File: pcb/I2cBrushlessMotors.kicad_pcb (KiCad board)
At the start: 2 copper layers, 50 x 50 mm, 65 parts, among them J1 Conn_01x03, J2 Conn_01x06, J3 Header, J4 Socket, J5 Conn_01x03, Q1 Q_PMOS_GSD, Q10 Q_PMOS_GSD, Q11 Q_NMOS_GSD, Q12 Q_NMOS_GSD, Q13 Q_PMOS_GSD, Q14 Q_NMOS_GSD, Q15 Q_NMOS_GSD, Q16 Q_PMOS_GSD, Q17 Q_NMOS_GSD, Q18 Q_NMOS_GSD, Q2 Q_NMOS_GSD, Q3 Q_NMOS_GSD, Q4 Q_PMOS_GSD, Q5 Q_NMOS_GSD, Q6 Q_NMOS_GSD, Q7 Q_PMOS_GSD, Q8 Q_NMOS_GSD, Q9 Q_NMOS_GSD, U1 ATmega328PB-MU

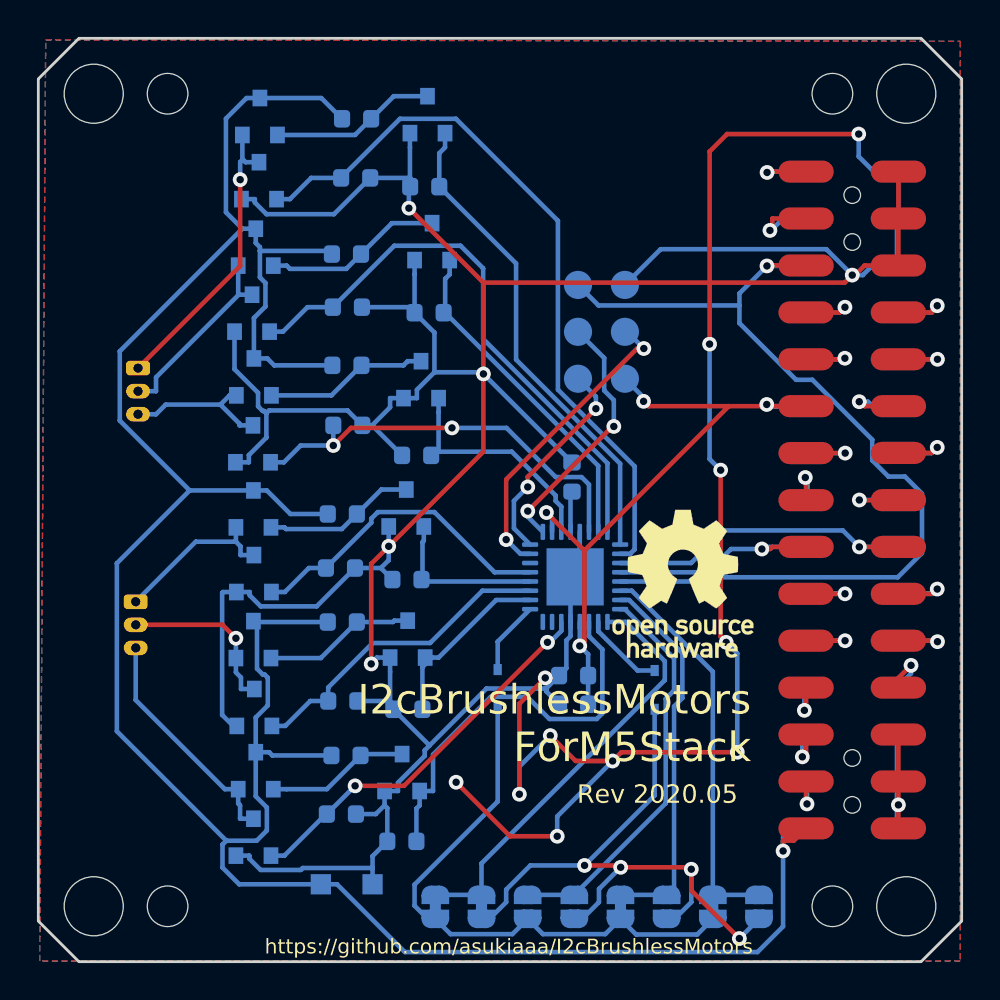
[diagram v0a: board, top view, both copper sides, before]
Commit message: Apply vertical connector
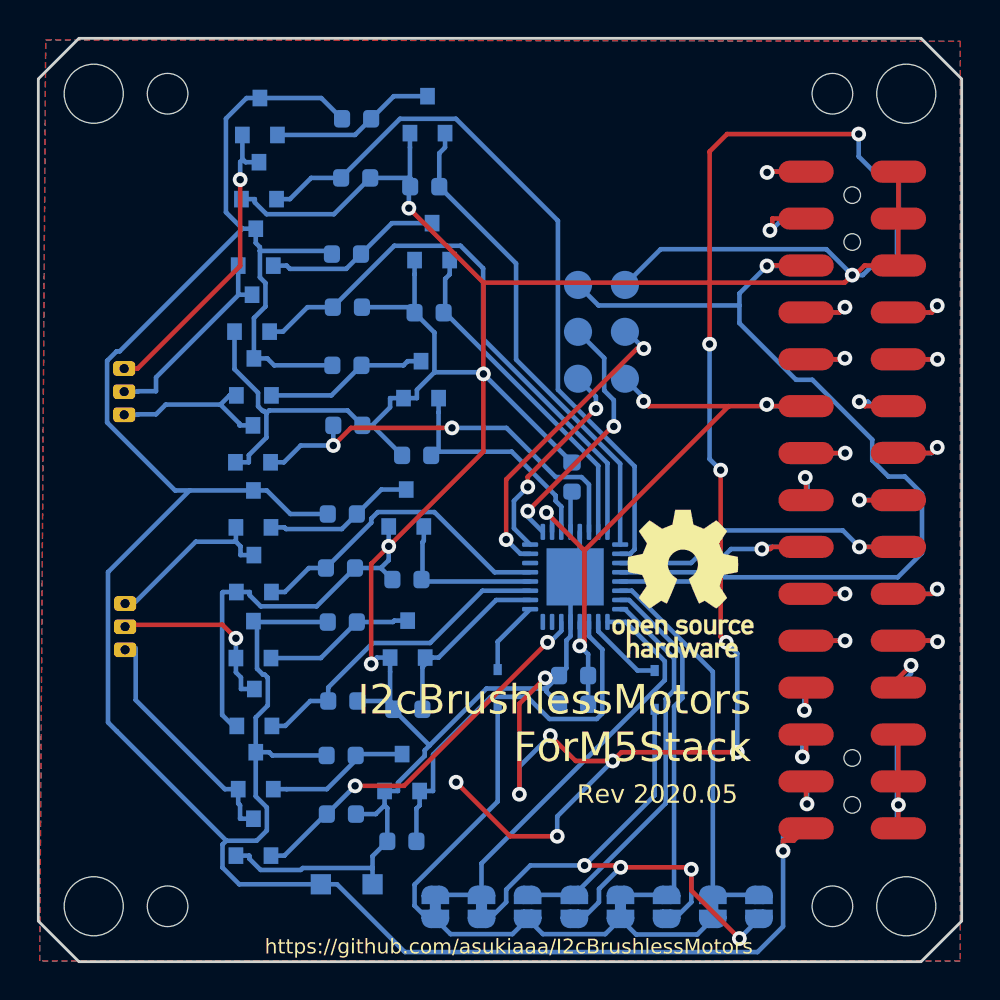
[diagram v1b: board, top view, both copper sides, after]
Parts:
- J1, J5: footprint Connector_Molex:Molex_PicoBlade_53047-0310_1x03_P1.25mm_Vertical -> footprints:Molex_1x03_P1.25mm_Vertical
- moved J5 2.76 mm to (102.9, 69.1)
- moved J1 2.65 mm to (103.0, 81.9)
- moved R7 0.26 mm to (116.4, 88.8)
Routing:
- net +BATT: track 145.5 -> 147.1 mm
- net /M2C: track 8.03 -> 8.79 mm
- net /M2B: track 10.4 -> 11.1 mm
- net /M2A: track 15.9 -> 16.7 mm
